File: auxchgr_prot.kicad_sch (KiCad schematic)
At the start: 6 parts, among them Q10 DMP3068L-7, Q8 DMP3068L-7, Q9 DMP3068L-7

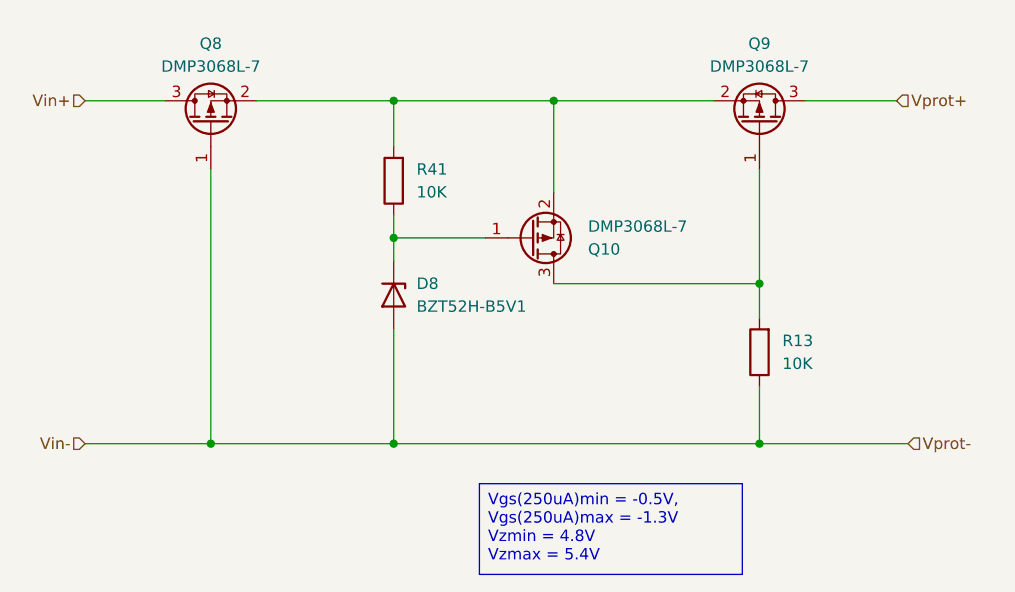
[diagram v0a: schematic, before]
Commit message: Change protection FETs and add resistor.
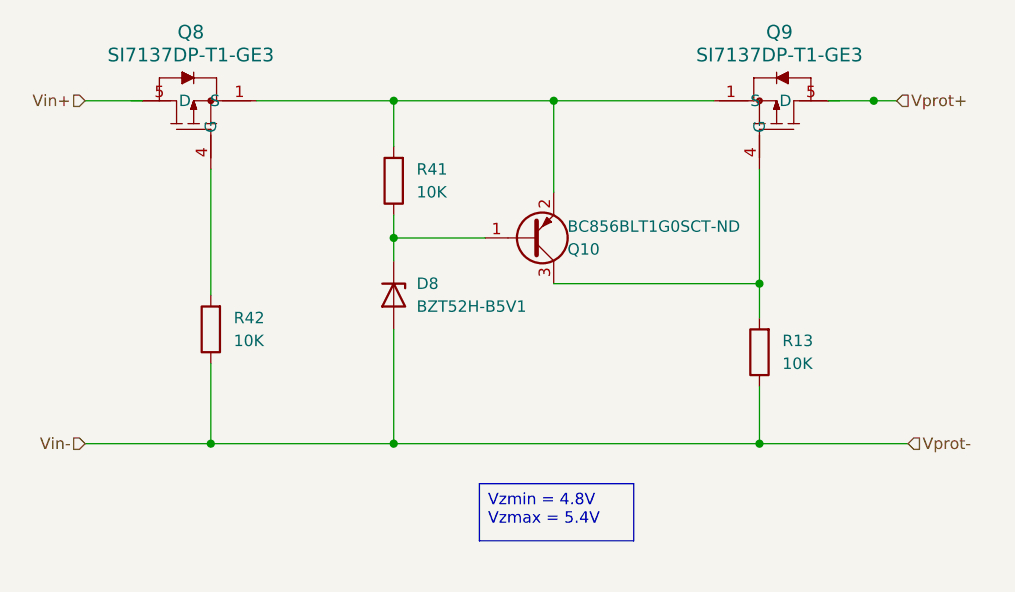
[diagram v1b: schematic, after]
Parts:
- removed Q10, Q8, Q9: DMP3068L-7, Package_TO_SOT_SMD:SOT-23, symbol Transistor_FET:DMP3099L
- added Q10: BC856BLT1G0SCT-ND, Package_TO_SOT_SMD:SOT-23, symbol Transistor_BJT:BC856
- added Q8, Q9: SI7137DP-T1-GE3, custom:MOSFET_7DP-T1-GE3_VIS, symbol custom:SI7137DP-T1-GE3
- added R42: 10K, Resistor_SMD:R_0603_1608Metric_Pad0.98x0.95mm_HandSolder, symbol Device:R
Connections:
- net Vin+: now also Q8.5 (D)
- net Vin-: now also R42.1
- net Vprot+: now also Q9.5 (D), Q9.6 (D), Q9.7 (D), Q9.8 (D)
- net at R41.2: now also Q10.2 (E), Q8.1 (S), Q9.1 (S)
- net at D8.1 (K), R41.1: now also Q10.1 (B)
- net at R13.2: now also Q10.3 (C), Q9.4 (G)
- new net: Q9.2 (S), Q9.3 (S)
- new net: Q8.4 (G), R42.2
- new net: Q8.2 (S), Q8.3 (S)
- new net: Q8.6 (D), Q8.7 (D), Q8.8 (D)

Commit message: Add wiring, change footprint to avoid fatal errors at pads.
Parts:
- renumbered Q9 to Q10, Q10 to Q9, R42 to R40, R13 to R42
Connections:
- net Vin+: now also Q8.6 (D), Q8.7 (D), Q8.8 (D)
- net at Q10.1 (S), Q8.1 (S), Q9.2 (E)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: now also Q10.2 (S), Q10.3 (S), Q8.2 (S), Q8.3 (S)
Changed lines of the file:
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@@
-	)
-	(junction
-		(at 129.54 25.4)
-		(diameter 0)
-		(color 0 0 0 0)
 	)
 	(junction
@@
 	(wire
 		(pts
+			(xy 41.91 25.4) (xy 46.99 25.4)
+		)
+		(stroke
+			(width 0)
+			(type default)
+		)
+	)
+	(wire
+		(pts
 			(xy 55.88 33.02) (xy 55.88 46.99)
 		)
@@
 	(wire
 		(pts
-			(xy 124.46 25.4) (xy 129.54 25.4)
-		)
-		(stroke
-			(width 0)
-			(type default)
-		)
-	)
-	(wire
-		(pts
 			(xy 76.2 25.4) (xy 93.98 25.4)
 		)
@@
 	(wire
 		(pts
-			(xy 129.54 25.4) (xy 132.08 25.4)
-		)
-		(stroke
-			(width 0)
-			(type default)
-		)
-	)
-	(wire
-		(pts
 			(xy 93.98 25.4) (xy 111.76 25.4)
 		)
@@
 	(wire
 		(pts
-			(xy 41.91 25.4) (xy 48.26 25.4)
+			(xy 125.73 25.4) (xy 132.08 25.4)
 		)
 		(stroke
@@
 		(dnp no)
 		(fields_autoplaced yes)
-		(property "Reference" "Q9"
+		(property "Reference" "Q10"
 			(at 119.0625 17.78 90)
 			(show_name no)
@@
 			(project "MoistureESP"
 				(path "/f2b9f638-139e-46ec-aa60-77c4af989196/0811c99d-47a8-481e-b182-179220f41fae"
-					(reference "Q9")
+					(reference "Q10")
 					(unit 1)
 				)
@@
 		(dnp no)
 		(fields_autoplaced yes)
-		(property "Reference" "R13"
+		(property "Reference" "R42"
 			(at 119.38 52.0699 0)
 			(show_name no)
@@
 			(project "MoistureESP"
 				(path "/f2b9f638-139e-46ec-aa60-77c4af989196/0811c99d-47a8-481e-b182-179220f41fae"
-					(reference "R13")
+					(reference "R42")
 					(unit 1)
 				)
@@
 		(dnp no)
 		(fields_autoplaced yes)
-		(property "Reference" "R42"
+		(property "Reference" "R40"
 			(at 58.42 49.5299 0)
 			(show_name no)
@@
 			(project "MoistureESP"
 				(path "/f2b9f638-139e-46ec-aa60-77c4af989196/0811c99d-47a8-481e-b182-179220f41fae"
-					(reference "R42")
+					(reference "R40")
 					(unit 1)
 				)
@@
 		(in_pos_files yes)
 		(dnp no)
-		(property "Reference" "Q10"
+		(property "Reference" "Q9"
 			(at 95.504 41.91 0)
 			(show_name no)
@@
 			(project "MoistureESP"
 				(path "/f2b9f638-139e-46ec-aa60-77c4af989196/0811c99d-47a8-481e-b182-179220f41fae"
-					(reference "Q10")
+					(reference "Q9")
 					(unit 1)
 				)

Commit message: Change USB charger position, redraw the zones.
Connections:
- net Vin+: no longer Q8.6 (D), Q8.7 (D), Q8.8 (D)
- net Vprot+: no longer Q10.6 (D), Q10.7 (D), Q10.8 (D)
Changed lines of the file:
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@@
 			)
-		)
-		(pin "8"
 		)
 		(pin "5"
@@
 		(pin "4"
 		)
-		(pin "7"
-		)
-		(pin "2"
-		)
-		(pin "6"
+		(pin "2"
 		)
 		(instances
@@
 	)
 	(symbol
+		(lib_name "SI7137DP-T1-GE3_1")
 		(lib_id "custom:SI7137DP-T1-GE3")
 		(at 54.61 25.4 270)
@@
 			)
 		)
-		(pin "8"
-		)
 		(pin "5"
 		)
@@
 		(pin "4"
 		)
-		(pin "7"
-		)
-		(pin "2"
-		)
-		(pin "6"
-		)
-		(instances
+		(pin "2"
+		)
+		(instances

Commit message: Export BOM, change page headers.
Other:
- company: (none) -> B.Major
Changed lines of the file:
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@@
 	(generator_version "10.0")
 	(paper "A4")
+	(title_block
+		(date "2026-03-27")
+		(rev "1")
+		(company "B.Major")
+	)
 	(text_box "Vzmin = 4.8V\nVzmax = 5.4V"
 		(exclude_from_sim no)
